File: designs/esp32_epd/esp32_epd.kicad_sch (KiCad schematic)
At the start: 8 parts, among them J1 Conn_01x12, J2 Conn_01x16, J3 XF2M-2415-1A

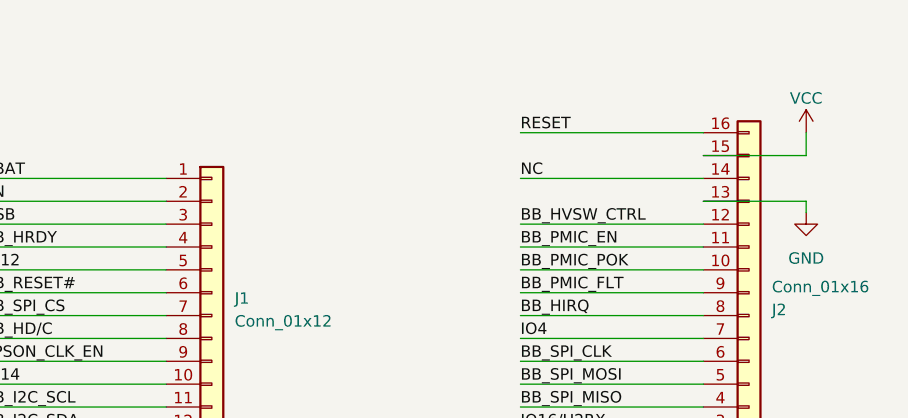
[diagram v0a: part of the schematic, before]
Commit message: Fix PCB sch and layout with VCC->VBAT
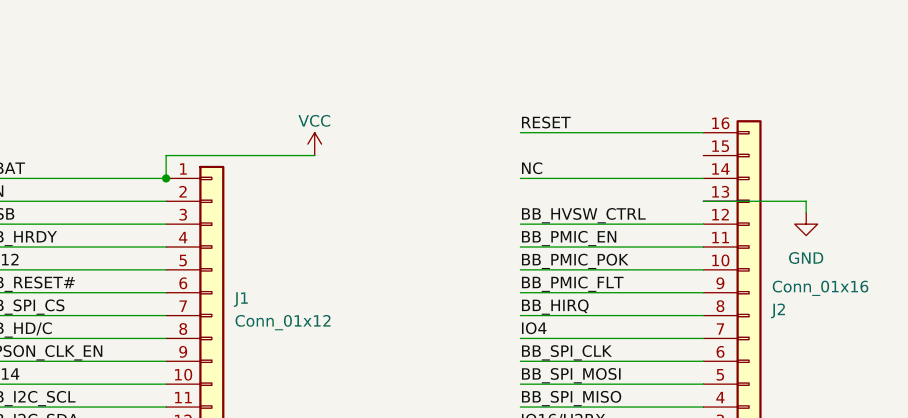
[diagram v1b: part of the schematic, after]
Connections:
- net VBAT is gone; now on net VCC: J1.1 (Pin_1)
- net VCC: no longer J2.15 (Pin_15)
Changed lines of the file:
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@@
   (junction (at 80.01 128.27) (diameter 0) (color 0 0 0 0)
   )
+  (junction (at 201.93 86.36) (diameter 0) (color 0 0 0 0)
+  )
   (junction (at 80.01 74.93) (diameter 0) (color 0 0 0 0)
   )
@@
   (junction (at 80.01 130.81) (diameter 0) (color 0 0 0 0)
   )
+  (wire (pts (xy 218.44 83.82) (xy 201.93 83.82))
+    (stroke (width 0) (type default))
+  )
   (wire (pts (xy 116.84 115.57) (xy 132.08 115.57))
     (stroke (width 0) (type default))
@@
     (stroke (width 0) (type default))
   )
-  (wire (pts (xy 273.05 83.82) (xy 261.62 83.82))
-    (stroke (width 0) (type default))
-  )
   (wire (pts (xy 80.01 80.01) (xy 80.01 82.55))
     (stroke (width 0) (type default))
@@
     (stroke (width 0) (type default))
   )
-  (wire (pts (xy 273.05 81.28) (xy 273.05 83.82))
-    (stroke (width 0) (type default))
-  )
   (wire (pts (xy 80.01 130.81) (xy 80.01 133.35))
     (stroke (width 0) (type default))
@@
   )
   (wire (pts (xy 52.07 105.41) (xy 80.01 105.41))
+    (stroke (width 0) (type default))
+  )
+  (wire (pts (xy 201.93 83.82) (xy 201.93 86.36))
     (stroke (width 0) (type default))
   )
@@
         (path "/c4ef1b35-4ca8-471a-96dc-191756c08869"
           (reference "RP2") (unit 1)
+        )
+      )
+    )
+  )
+  (symbol (lib_id "power:VCC") (at 218.44 83.82 0) (unit 1)
+    (in_bom yes) (on_board yes) (dnp no)
+    (property "Reference" "#PWR03" (at 218.44 87.63 0)
+      (effects (font (size 1.27 1.27)) hide)
+    )
+    (property "Value" "VCC" (at 218.44 80.01 0)
+      (effects (font (size 1.27 1.27)))
+    )
+    (property "Footprint" "" (at 218.44 83.82 0)
+      (effects (font (size 1.27 1.27)) hide)
+    )
+    (property "Datasheet" "" (at 218.44 83.82 0)
+      (effects (font (size 1.27 1.27)) hide)
+    )
+    (pin "1")
+    (instances
+      (project "esp32_epd"
+        (path "/c4ef1b35-4ca8-471a-96dc-191756c08869"
+          (reference "#PWR03") (unit 1)
         )
       )
@@
         )
       )
-    )
-  )
-  (symbol (lib_id "power:VCC") (at 273.05 81.28 0) (unit 1)
-    (in_bom yes) (on_board yes) (dnp no)
-    (property "Reference" "#PWR03" (at 273.05 85.09 0)
-      (effects (font (size 1.27 1.27)) hide)
-    )
-    (property "Value" "VCC" (at 273.05 77.47 0)
-      (effects (font (size 1.27 1.27)))
-    )
-    (property "Footprint" "" (at 273.05 81.28 0)
-      (effects (font (size 1.27 1.27)) hide)
-    )
-    (property "Datasheet" "" (at 273.05 81.28 0)
-      (effects (font (size 1.27 1.27)) hide)
-    )
-    (pin "1")
-    (instances
-      (project "esp32_epd"
-        (path "/c4ef1b35-4ca8-471a-96dc-191756c08869"
-          (reference "#PWR03") (unit 1)
-        )
-      )
